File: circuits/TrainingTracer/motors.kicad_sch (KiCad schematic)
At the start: 6 parts, among them J4 DRV8835_1, J5 DRV8835_2, J6 PINHD-1x6, J7 PINHD-1x6

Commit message: 回路完成
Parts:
- J14: renamed from J4; footprint (none) -> Connector_PinSocket_2.54mm:PinSocket_1x06_P2.54mm_Vertical
- J15: renamed from J5; footprint (none) -> Connector_PinSocket_2.54mm:PinSocket_1x06_P2.54mm_Vertical
- J16: renamed from J6; value PINHD-1x6 -> PINHD-1x6(MOTOR-L); footprint (none) -> Connector_PinSocket_2.54mm:PinSocket_1x06_P2.54mm_Vertical
- J17: renamed from J7; value PINHD-1x6 -> PINHD-1x6(MOTO-R); footprint (none) -> Connector_PinSocket_2.54mm:PinSocket_1x06_P2.54mm_Vertical
- R16, R17: value R_Small_US -> 10k; footprint (none) -> Resistor_THT:R_Axial_DIN0204_L3.6mm_D1.6mm_P7.62mm_Horizontal
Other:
- moved on the sheet: J17

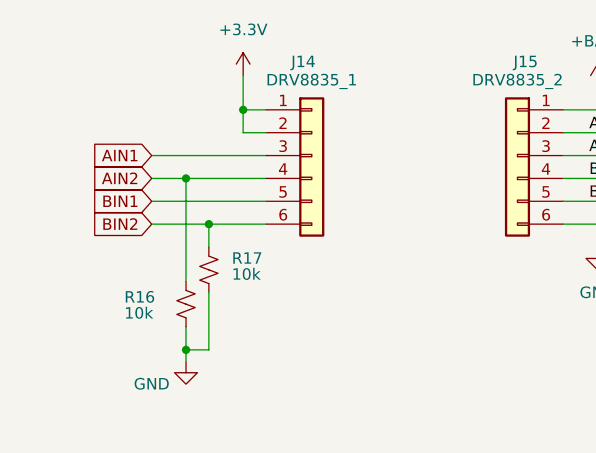
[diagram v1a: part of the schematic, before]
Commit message: PCBのPDF出力
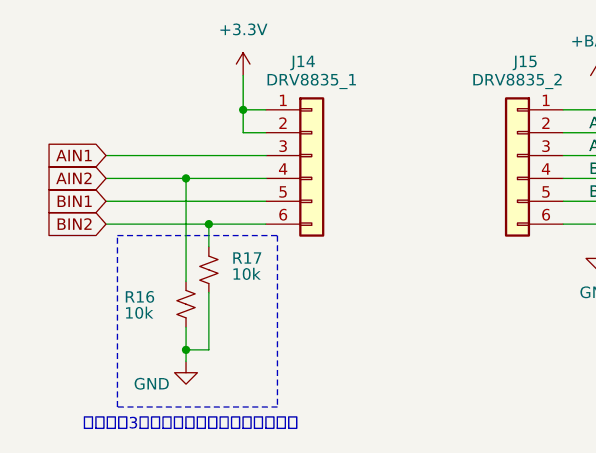
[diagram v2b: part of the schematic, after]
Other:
- note added: "改良箇所3：マイコンブート前の暴走対策"
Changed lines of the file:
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@@
 	(generator_version "9.0")
 	(paper "A4")
+	(rectangle
+		(start 82.55 102.87)
+		(end 100.33 121.92)
+		(stroke
+			(width 0)
+			(type dash)
+		)
+		(fill
+			(type none)
+		)
+	)
+	(text "改良箇所3：マイコンブート前の暴走対策"
+		(exclude_from_sim no)
+		(at 90.678 123.952 0)
+		(effects
+			(font
+				(size 1.27 1.27)
+			)
+		)
+	)
 	(junction
 		(at 96.52 88.9)
@@
 	(wire
 		(pts
-			(xy 86.36 99.06) (xy 99.06 99.06)
+			(xy 81.28 99.06) (xy 99.06 99.06)
 		)
 		(stroke
@@
 	(wire
 		(pts
-			(xy 86.36 93.98) (xy 99.06 93.98)
+			(xy 81.28 93.98) (xy 99.06 93.98)
 		)
 		(stroke
@@
 	(wire
 		(pts
-			(xy 86.36 101.6) (xy 92.71 101.6)
+			(xy 81.28 101.6) (xy 92.71 101.6)
 		)
 		(stroke
@@
 	(wire
 		(pts
-			(xy 86.36 96.52) (xy 90.17 96.52)
+			(xy 81.28 96.52) (xy 90.17 96.52)
 		)
 		(stroke
@@
 	(global_label "BIN1"
 		(shape input)
-		(at 86.36 99.06 180)
+		(at 81.28 99.06 180)
 		(fields_autoplaced yes)
 		(effects
@@
 		)
 		(property "Intersheetrefs" "${INTERSHEET_REFS}"
-			(at 78.96 99.06 0)
+			(at 73.88 99.06 0)
 			(effects
 				(font
@@
 	(global_label "AIN1"
 		(shape input)
-		(at 86.36 93.98 180)
+		(at 81.28 93.98 180)
 		(fields_autoplaced yes)
 		(effects
@@
 		)
 		(property "Intersheetrefs" "${INTERSHEET_REFS}"
-			(at 79.1414 93.98 0)
+			(at 74.0614 93.98 0)
 			(effects
 				(font
@@
 	(global_label "BIN2"
 		(shape input)
-		(at 86.36 101.6 180)
+		(at 81.28 101.6 180)
 		(fields_autoplaced yes)
 		(effects
@@
 		)
 		(property "Intersheetrefs" "${INTERSHEET_REFS}"
-			(at 78.96 101.6 0)
+			(at 73.88 101.6 0)
 			(effects
 				(font
@@
 	(global_label "AIN2"
 		(shape input)
-		(at 86.36 96.52 180)
+		(at 81.28 96.52 180)
 		(fields_autoplaced yes)
 		(effects
@@
 		)
 		(property "Intersheetrefs" "${INTERSHEET_REFS}"
-			(at 79.1414 96.52 0)
+			(at 74.0614 96.52 0)
 			(effects
 				(font
